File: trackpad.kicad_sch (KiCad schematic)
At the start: 0 parts

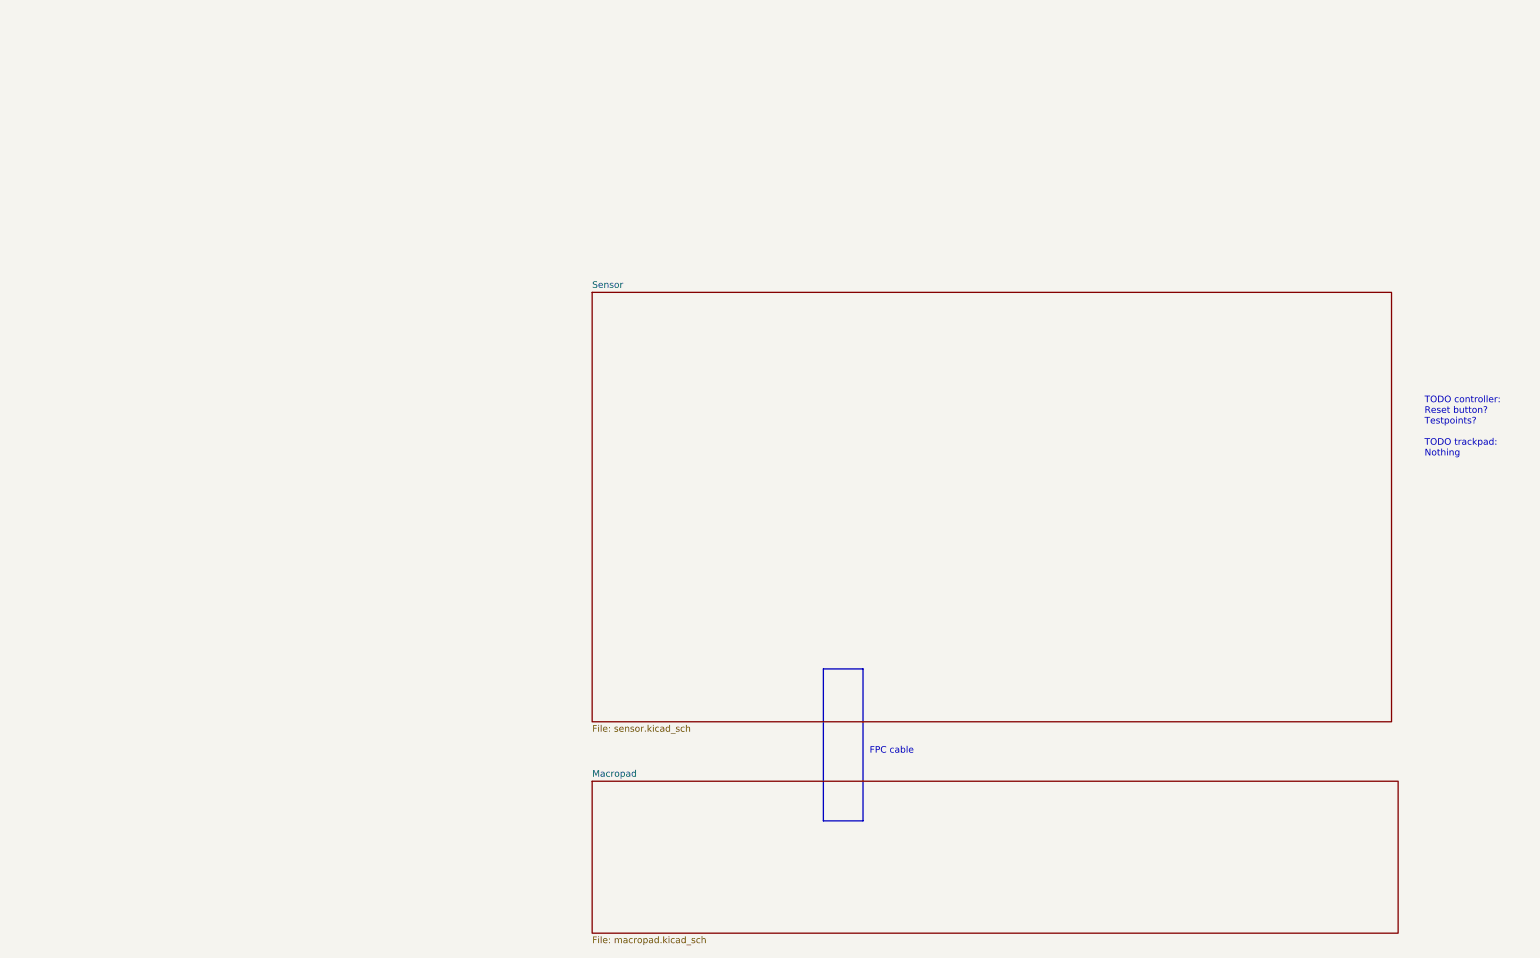
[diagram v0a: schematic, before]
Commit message: smashed everything into one PCB and removed some parts I don't want.
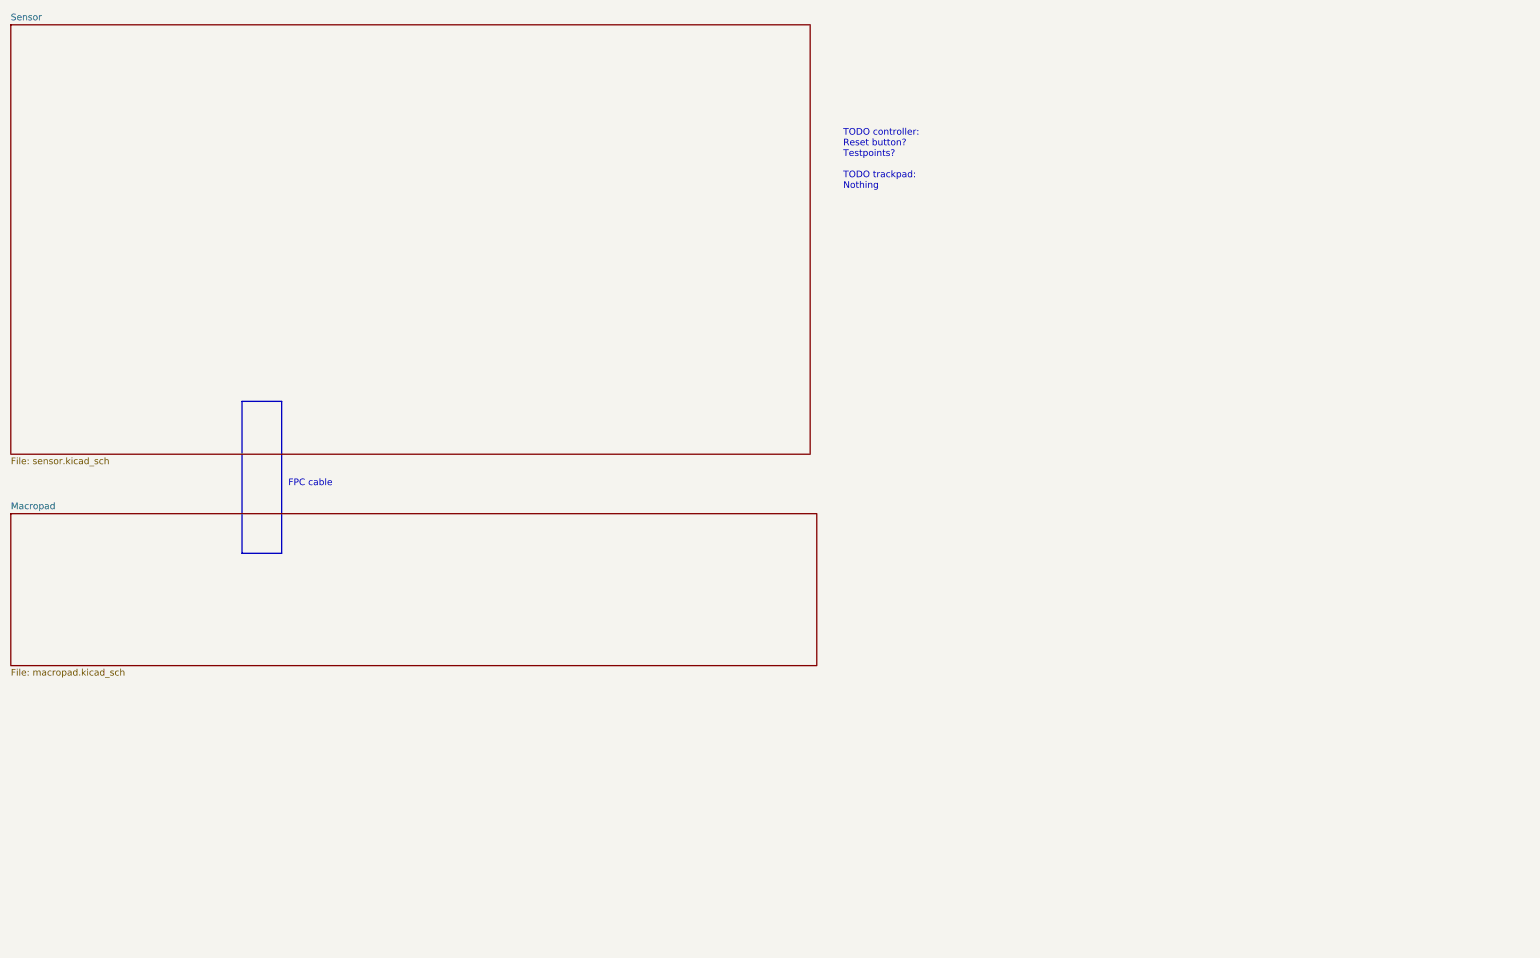
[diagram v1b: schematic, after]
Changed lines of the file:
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@@
 (kicad_sch (version 20230121) (generator eeschema)
-  (paper "A3")
+  (paper "A4")
   (title_block
     (title "Trackpad")
@@
     (company "George Norton")
   )
-  (rectangle (start 190.5 149.86) (end 198.12 179.07)
+  (rectangle (start 78.74 98.425) (end 86.36 127.635)
     (stroke (width 0) (type default))
     (fill (type none))
   )
   (text "TODO controller:\nReset button?\nTestpoints?\n\nTODO trackpad:\nNothing"
-    (at 306.07 109.22 0)
+    (at 194.31 57.785 0)
     (effects (font (size 1.27 1.27)) (justify left bottom))
   )
-  (text "FPC cable" (at 199.39 166.37 0)
+  (text "FPC cable" (at 87.63 114.935 0)
     (effects (font (size 1.27 1.27)) (justify left bottom))
   )
-  (sheet (at 146.05 77.47) (size 153.67 82.55) (fields_autoplaced)
+  (sheet (at 34.29 26.035) (size 153.67 82.55) (fields_autoplaced)
     (stroke (width 0.1524) (type solid))
     (fill (color 0 0 0 0.0000))
-    (property "Sheetname" "Sensor" (at 146.05 76.7584 0)
+    (property "Sheetname" "Sensor" (at 34.29 25.3234 0)
       (effects (font (size 1.27 1.27)) (justify left bottom))
     )
-    (property "Sheetfile" "sensor.kicad_sch" (at 146.05 160.6046 0)
+    (property "Sheetfile" "sensor.kicad_sch" (at 34.29 109.1696 0)
       (effects (font (size 1.27 1.27)) (justify left top))
     )
@@
     )
   )
-  (sheet (at 146.05 171.45) (size 154.94 29.21) (fields_autoplaced)
+  (sheet (at 34.29 120.015) (size 154.94 29.21) (fields_autoplaced)
     (stroke (width 0.1524) (type solid))
     (fill (color 0 0 0 0.0000))
-    (property "Sheetname" "Macropad" (at 146.05 170.7384 0)
+    (property "Sheetname" "Macropad" (at 34.29 119.3034 0)
       (effects (font (size 1.27 1.27)) (justify left bottom))
     )
-    (property "Sheetfile" "macropad.kicad_sch" (at 146.05 201.2446 0)
+    (property "Sheetfile" "macropad.kicad_sch" (at 34.29 149.8096 0)
       (effects (font (size 1.27 1.27)) (justify left top))
     )
